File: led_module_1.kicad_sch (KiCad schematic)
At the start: 10 parts, among them U5 74HC595

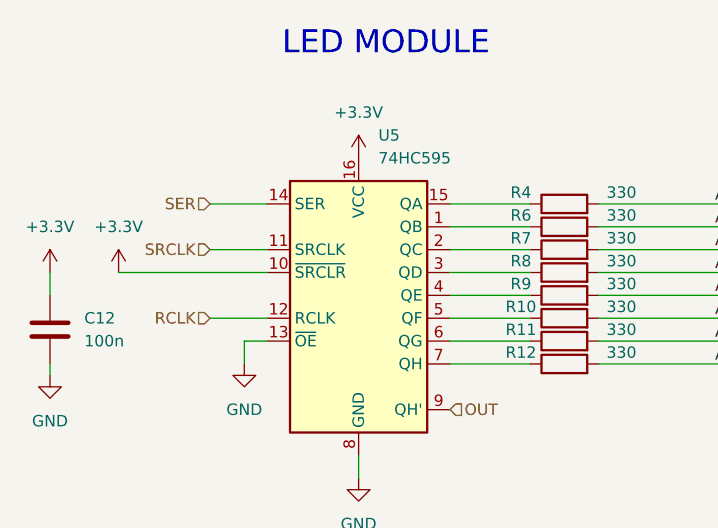
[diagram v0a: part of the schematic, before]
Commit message: LED updates with some layout
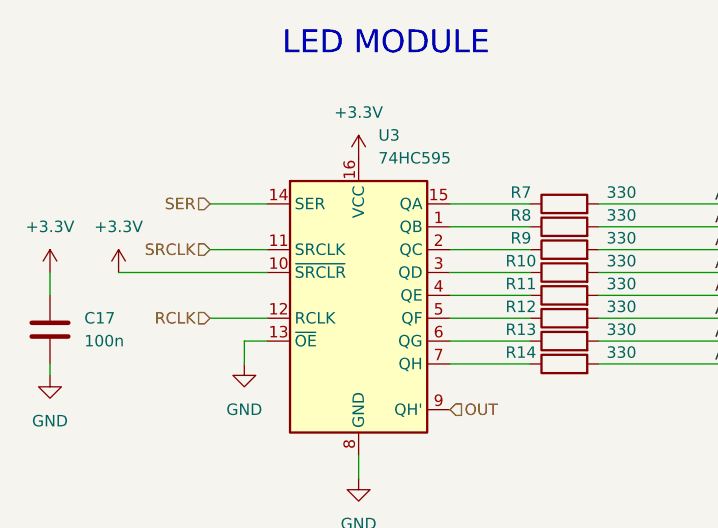
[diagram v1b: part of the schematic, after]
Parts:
- renumbered C12 to C17, R8 to R10, R9 to R11, R10 to R12, R11 to R13, R12 to R14, R4 to R7, R6 to R8, R7 to R9, U5 to U3

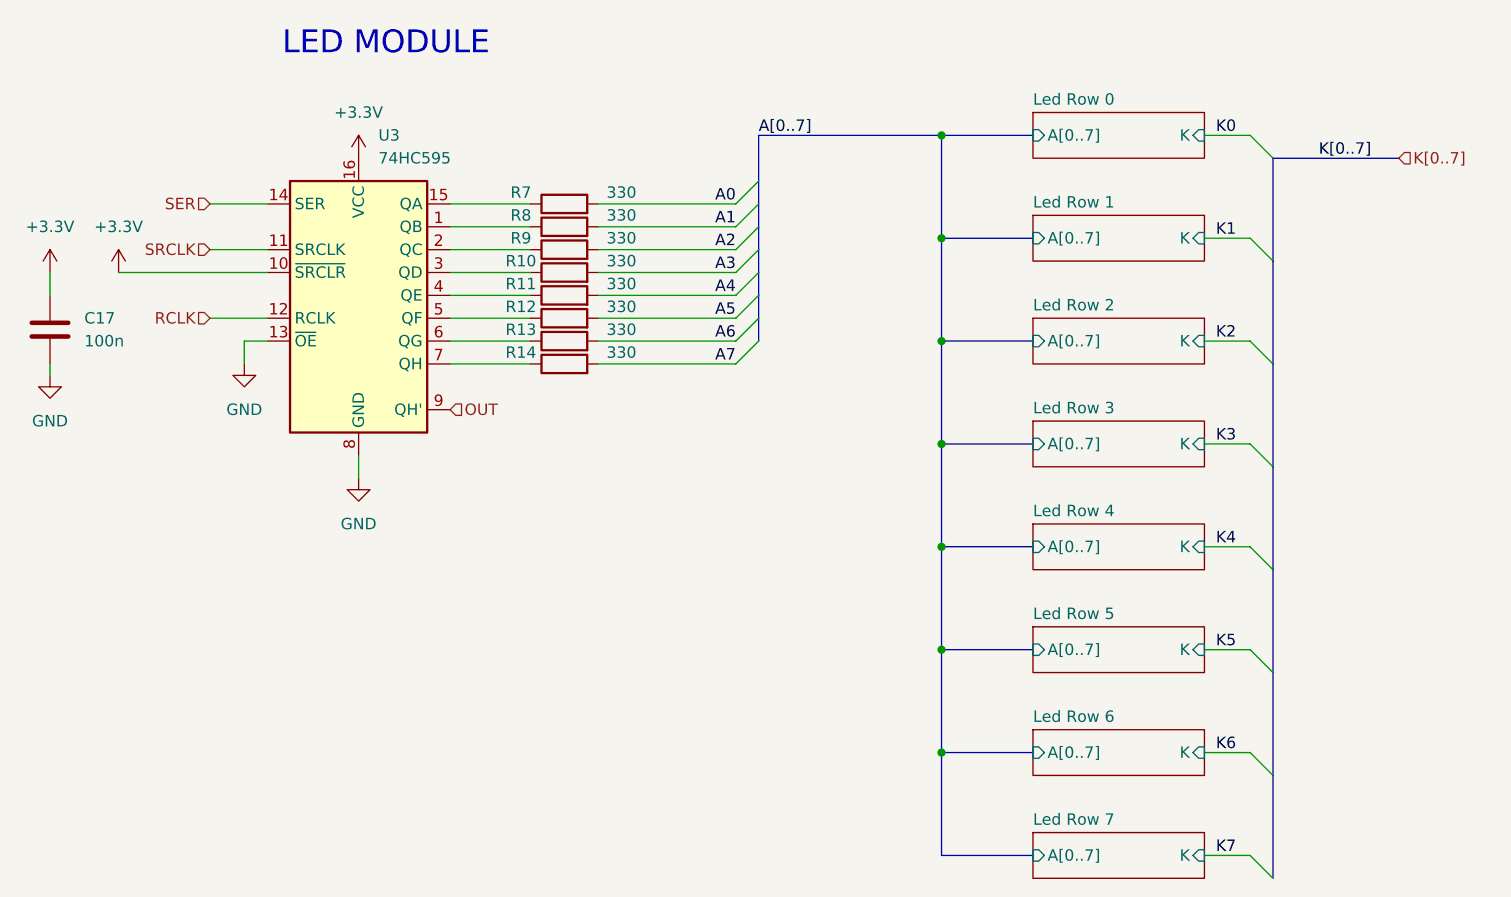
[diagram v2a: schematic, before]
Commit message: Relabeled MOSFETs
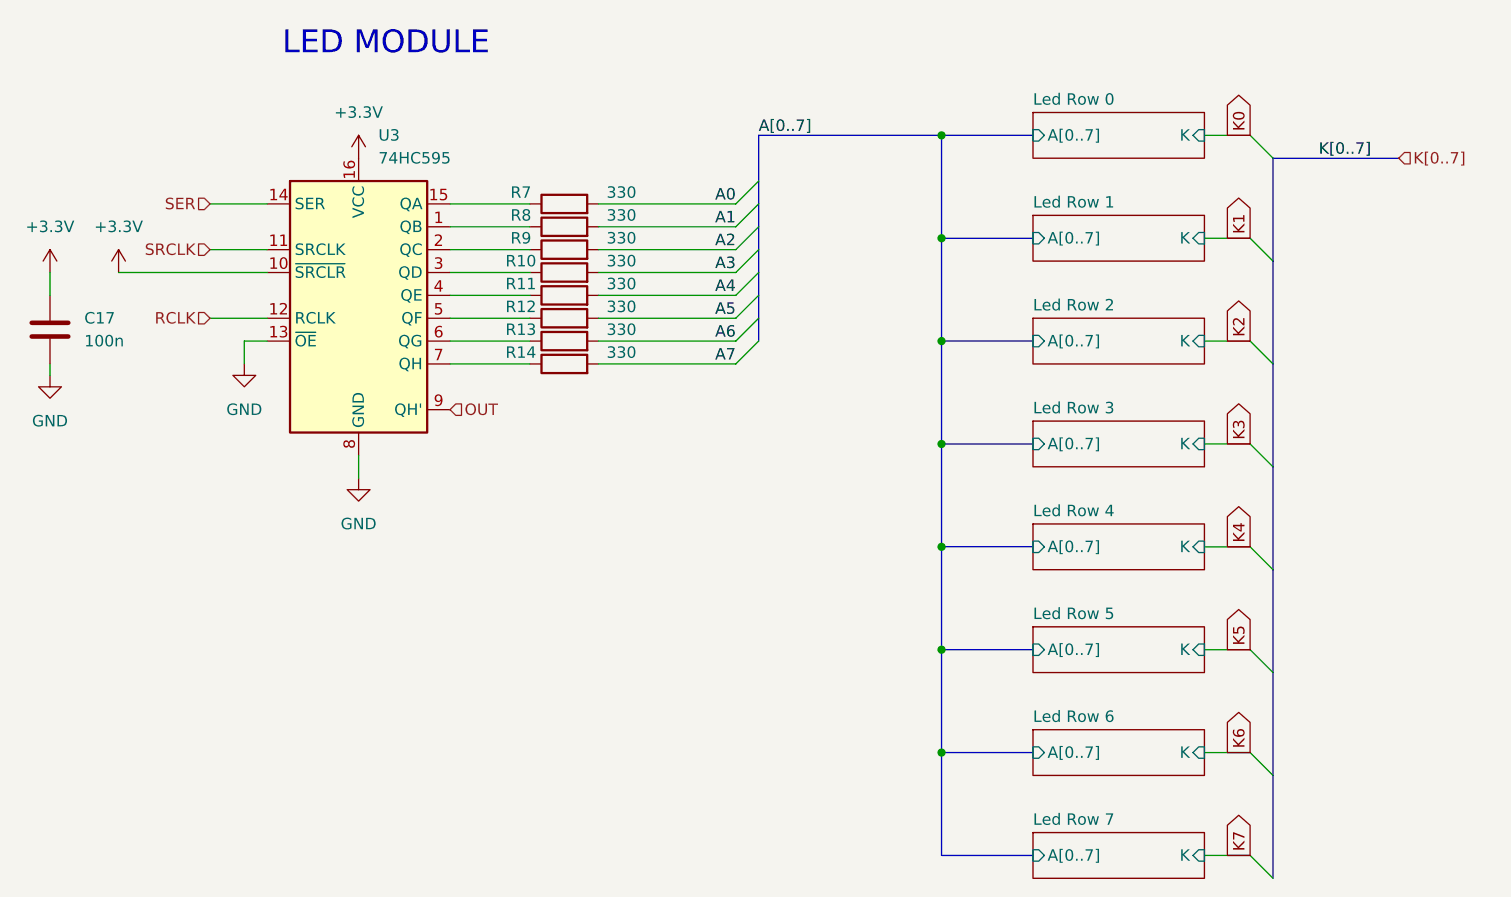
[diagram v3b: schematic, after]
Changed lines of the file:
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@@
-		)
-	)
-	(label "K2"
-		(at 148.59 60.96 0)
-		(effects
-			(font
-				(size 1.27 1.27)
-			)
-			(justify left bottom)
 		)
 	)
@@
 		)
 	)
-	(label "K4"
-		(at 148.59 83.82 0)
-		(effects
-			(font
-				(size 1.27 1.27)
-			)
-			(justify left bottom)
-		)
-	)
-	(label "K5"
-		(at 148.59 95.25 0)
-		(effects
-			(font
-				(size 1.27 1.27)
-			)
-			(justify left bottom)
-		)
-	)
-	(label "K6"
-		(at 148.59 106.68 0)
-		(effects
-			(font
-				(size 1.27 1.27)
-			)
-			(justify left bottom)
-		)
-	)
-	(label "K3"
-		(at 148.59 72.39 0)
-		(effects
-			(font
-				(size 1.27 1.27)
-			)
-			(justify left bottom)
-		)
-	)
 	(label "K[0..7]"
 		(at 160.02 40.64 0)
@@
 		)
 	)
-	(label "K0"
-		(at 148.59 38.1 0)
-		(effects
-			(font
-				(size 1.27 1.27)
-			)
-			(justify left bottom)
-		)
-	)
 	(label "A[0..7]"
 		(at 97.79 38.1 0)
@@
 		)
 	)
-	(label "K7"
-		(at 148.59 118.11 0)
-		(effects
-			(font
-				(size 1.27 1.27)
-			)
-			(justify left bottom)
-		)
-	)
 	(label "A2"
 		(at 95.25 50.8 180)
@@
 		)
 	)
-	(label "K1"
-		(at 148.59 49.53 0)
-		(effects
-			(font
-				(size 1.27 1.27)
-			)
-			(justify left bottom)
-		)
-	)
 	(label "A5"
 		(at 95.25 58.42 180)
@@
 		)
 	)
+	(global_label "K5"
+		(shape output)
+		(at 151.13 95.25 90)
+		(fields_autoplaced yes)
+		(effects
+			(font
+				(size 1.27 1.27)
+			)
+			(justify left)
+		)
+		(property "Intersheetrefs" "${INTERSHEET_REFS}"
+			(at 151.13 89.7853 90)
+			(effects
+				(font
+					(size 1.27 1.27)
+				)
+				(justify left)
+				(hide yes)
+			)
+		)
+	)
+	(global_label "K2"
+		(shape output)
+		(at 151.13 60.96 90)
+		(fields_autoplaced yes)
+		(effects
+			(font
+				(size 1.27 1.27)
+			)
+			(justify left)
+		)
+		(property "Intersheetrefs" "${INTERSHEET_REFS}"
+			(at 151.13 55.4953 90)
+			(effects
+				(font
+					(size 1.27 1.27)
+				)
+				(justify left)
+				(hide yes)
+			)
+		)
+	)
+	(global_label "K7"
+		(shape output)
+		(at 151.13 118.11 90)
+		(fields_autoplaced yes)
+		(effects
+			(font
+				(size 1.27 1.27)
+			)
+			(justify left)
+		)
+		(property "Intersheetrefs" "${INTERSHEET_REFS}"
+			(at 151.13 112.6453 90)
+			(effects
+				(font
+					(size 1.27 1.27)
+				)
+				(justify left)
+				(hide yes)
+			)
+		)
+	)
+	(global_label "K0"
+		(shape output)
+		(at 151.13 38.1 90)
+		(fields_autoplaced yes)
+		(effects
+			(font
+				(size 1.27 1.27)
+			)
+			(justify left)
+		)
+		(property "Intersheetrefs" "${INTERSHEET_REFS}"
+			(at 151.13 32.6353 90)
+			(effects
+				(font
+					(size 1.27 1.27)
+				)
+				(justify left)
+				(hide yes)
+			)
+		)
+	)
+	(global_label "K1"
+		(shape output)
+		(at 151.13 49.53 90)
+		(fields_autoplaced yes)
+		(effects
+			(font
+				(size 1.27 1.27)
+			)
+			(justify left)
+		)
+		(property "Intersheetrefs" "${INTERSHEET_REFS}"
+			(at 151.13 44.0653 90)
+			(effects
+				(font
+					(size 1.27 1.27)
+				)
+				(justify left)
+				(hide yes)
+			)
+		)
+	)
+	(global_label "K3"
+		(shape output)
+		(at 151.13 72.39 90)
+		(fields_autoplaced yes)
+		(effects
+			(font
+				(size 1.27 1.27)
+			)
+			(justify left)
+		)
+		(property "Intersheetrefs" "${INTERSHEET_REFS}"
+			(at 151.13 66.9253 90)
+			(effects
+				(font
+					(size 1.27 1.27)
+				)
+				(justify left)
+				(hide yes)
+			)
+		)
+	)
+	(global_label "K6"
+		(shape output)
+		(at 151.13 106.68 90)
+		(fields_autoplaced yes)
+		(effects
+			(font
+				(size 1.27 1.27)
+			)
+			(justify left)
+		)
+		(property "Intersheetrefs" "${INTERSHEET_REFS}"
+			(at 151.13 101.2153 90)
+			(effects
+				(font
+					(size 1.27 1.27)
+				)
+				(justify left)
+				(hide yes)
+			)
+		)
+	)
+	(global_label "K4"
+		(shape output)
+		(at 151.13 83.82 90)
+		(fields_autoplaced yes)
+		(effects
+			(font
+				(size 1.27 1.27)
+			)
+			(justify left)
+		)
+		(property "Intersheetrefs" "${INTERSHEET_REFS}"
+			(at 151.13 78.3553 90)
+			(effects
+				(font
+					(size 1.27 1.27)
+				)
+				(justify left)
+				(hide yes)
+			)
+		)
+	)

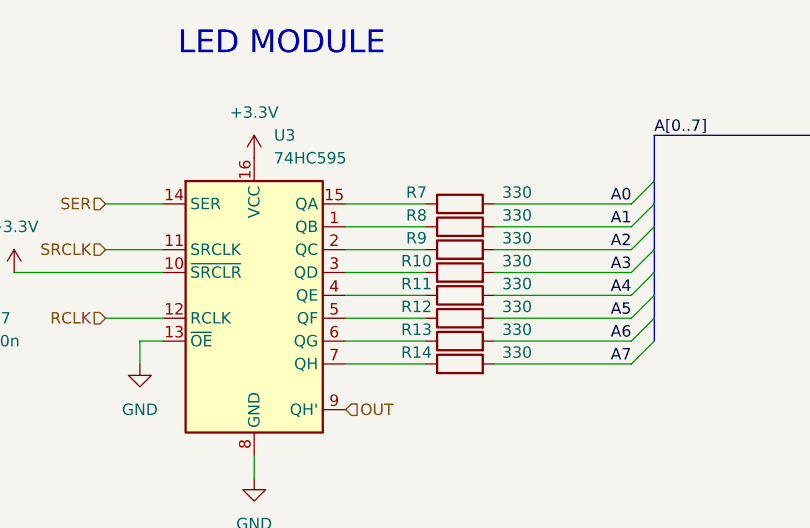
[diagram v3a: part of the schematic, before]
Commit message: Modified buck converter in schematic and pcb and got rid of old fabrication files
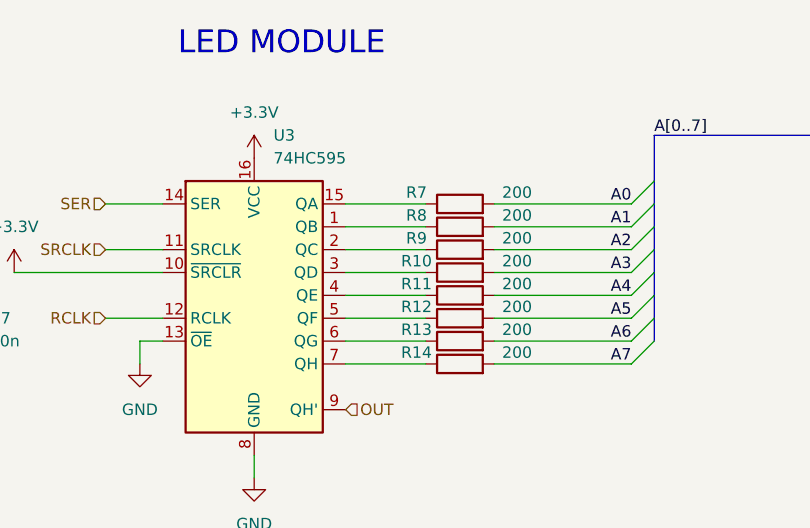
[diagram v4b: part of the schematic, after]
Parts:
- C17: LCSC (none) -> C1525
- R10, R11, R12, R13, R14, R7, R8, R9: value 330 -> 200; LCSC (none) -> C25087
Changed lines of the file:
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@@
+			)
+		)
+		(property "LCSC" "C1525 "
+			(at 19.05 59.69 0)
+			(effects
+				(font
+					(size 1.27 1.27)
+				)
+				(hide yes)
 			)
 		)
@@
 			)
 		)
-		(property "Value" "330"
+		(property "Value" "200"
 			(at 82.55 62.23 90)
 			(effects
@@
 		(property "Description" "Resistor"
 			(at 76.2 63.5 0)
+			(effects
+				(font
+					(size 1.27 1.27)
+				)
+				(hide yes)
+			)
+		)
+		(property "LCSC" "C25087"
+			(at 76.2 63.5 90)
 			(effects
 				(font
@@
 			)
 		)
-		(property "Value" "330"
+		(property "Value" "200"
 			(at 82.55 57.15 90)
 			(effects
@@
 		(property "Description" "Resistor"
 			(at 76.2 58.42 0)
+			(effects
+				(font
+					(size 1.27 1.27)
+				)
+				(hide yes)
+			)
+		)
+		(property "LCSC" "C25087"
+			(at 76.2 58.42 90)
 			(effects
 				(font
@@
 			)
 		)
-		(property "Value" "330"
+		(property "Value" "200"
 			(at 82.55 46.99 90)
 			(effects
@@
 		(property "Description" "Resistor"
 			(at 76.2 48.26 0)
+			(effects
+				(font
+					(size 1.27 1.27)
+				)
+				(hide yes)
+			)
+		)
+		(property "LCSC" "C25087"
+			(at 76.2 48.26 90)
 			(effects
 				(font
@@
 			)
 		)
-		(property "Value" "330"
+		(property "Value" "200"
 			(at 82.55 59.69 90)
 			(effects
@@
 		(property "Description" "Resistor"
 			(at 76.2 60.96 0)
+			(effects
+				(font
+					(size 1.27 1.27)
+				)
+				(hide yes)
+			)
+		)
+		(property "LCSC" "C25087"
+			(at 76.2 60.96 90)
 			(effects
 				(font
@@
 			)
 		)
-		(property "Value" "330"
+		(property "Value" "200"
 			(at 82.55 44.45 90)
 			(effects
@@
 		(property "Description" "Resistor"
 			(at 76.2 45.72 0)
+			(effects
+				(font
+					(size 1.27 1.27)
+				)
+				(hide yes)
+			)
+		)
+		(property "LCSC" "C25087"
+			(at 76.2 45.72 90)
 			(effects
 				(font
@@
 			)
 		)
-		(property "Value" "330"
+		(property "Value" "200"
 			(at 82.55 52.07 90)
 			(effects
@@
 		(property "Description" "Resistor"
 			(at 76.2 53.34 0)
+			(effects
+				(font
+					(size 1.27 1.27)
+				)
+				(hide yes)
+			)
+		)
+		(property "LCSC" "C25087"
+			(at 76.2 53.34 90)
 			(effects
 				(font
@@
 			)
 		)
-		(property "Value" "330"
+		(property "Value" "200"
 			(at 82.55 49.53 90)
 			(effects
@@
 		(property "Description" "Resistor"
 			(at 76.2 50.8 0)
+			(effects
+				(font
+					(size 1.27 1.27)
+				)
+				(hide yes)
+			)
+		)
+		(property "LCSC" "C25087"
+			(at 76.2 50.8 90)
 			(effects
 				(font
@@
 			)
 		)
-		(property "Value" "330"
+		(property "Value" "200"
 			(at 82.55 54.61 90)
 			(effects
@@
 		(property "Description" "Resistor"
 			(at 76.2 55.88 0)
+			(effects
+				(font
+					(size 1.27 1.27)
+				)
+				(hide yes)
+			)
+		)
+		(property "LCSC" "C25087"
+			(at 76.2 55.88 90)
 			(effects
 				(font
@@
 		(fields_autoplaced yes)
 		(property "Reference" "U3"
-			(at 55.5341 38.1 0)
+			(at 55.4833 38.1 0)
 			(effects
 				(font
@@
 		)
 		(property "Value" "74HC595"
-			(at 55.5341 40.64 0)
-			(effects
-				(font
+			(at 55.4833 40.64 0)
+			(effects
+				(font

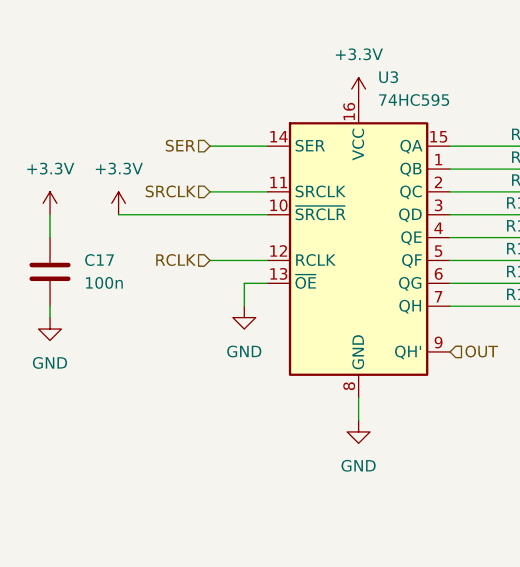
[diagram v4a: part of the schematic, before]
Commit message: Updated usb-micro, have filled in all LCSC fields
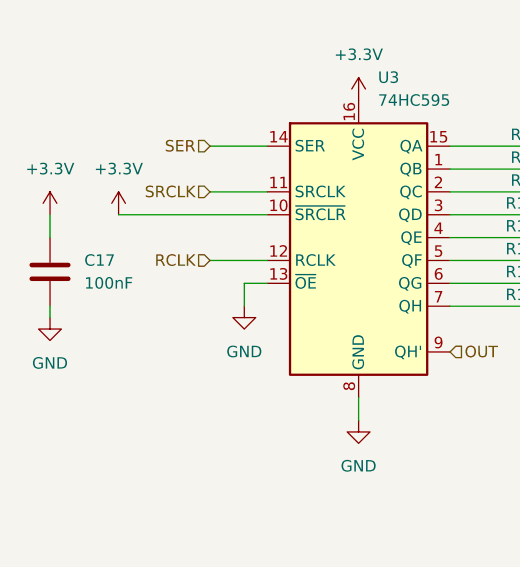
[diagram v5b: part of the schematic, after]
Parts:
- C17: value 100n -> 100nF; LCSC C1525 -> C1525
- U3: LCSC (none) -> C5947
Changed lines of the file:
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@@
 			)
 		)
-		(property "Value" "100n"
+		(property "Value" "100nF"
 			(at 22.86 60.9599 0)
 			(effects
@@
 			)
 		)
-		(property "LCSC" "C1525 "
+		(property "LCSC" "C1525"
 			(at 19.05 59.69 0)
 			(effects
@@
 			(at 53.34 55.88 0)
 			(effects
+				(font
+					(size 1.27 1.27)
+				)
+				(hide yes)
+			)
+		)
+		(property "LCSC" "C5947"
+			(at 53.34 55.88 0)
+			(effects
